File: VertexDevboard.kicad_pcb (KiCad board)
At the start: 2 copper layers, 21 x 51 mm, 33 parts, among them J1 USB_C_Receptacle_USB2.0_14P, J2 Conn_01x20, J3 Conn_01x20, J4 Conn_01x03, SW1 SW_Push, U1 RP2040, U2 MCP1700x-330xxTT, U3 W25Q128JVS, Y1 12 MHz

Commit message: DRC OK
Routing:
- net QSPI_SS: track 63.0 -> 61.0 mm
- net +3V3: track 106.9 -> 105.2 mm, vias 9 -> 8
- net GPIO23: track 11.1 -> 10.3 mm
- net GPIO22: track 7.42 -> 6.82 mm
- net XOUT: track 5.75 -> 5.22 mm
- net GPIO2: track 27.0 -> 26.5 mm
- net GPIO13: vias 3 -> 1
- net GND: vias 22 -> 21

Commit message: Before fabric
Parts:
- added G***: LOGO, LOGO, F.Cu at (127.0, 126.0)
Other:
- board text added: "Shauli Sultan"
- board text added: "Vertex DevBoard"
- board text added: "Vertex Devboard"

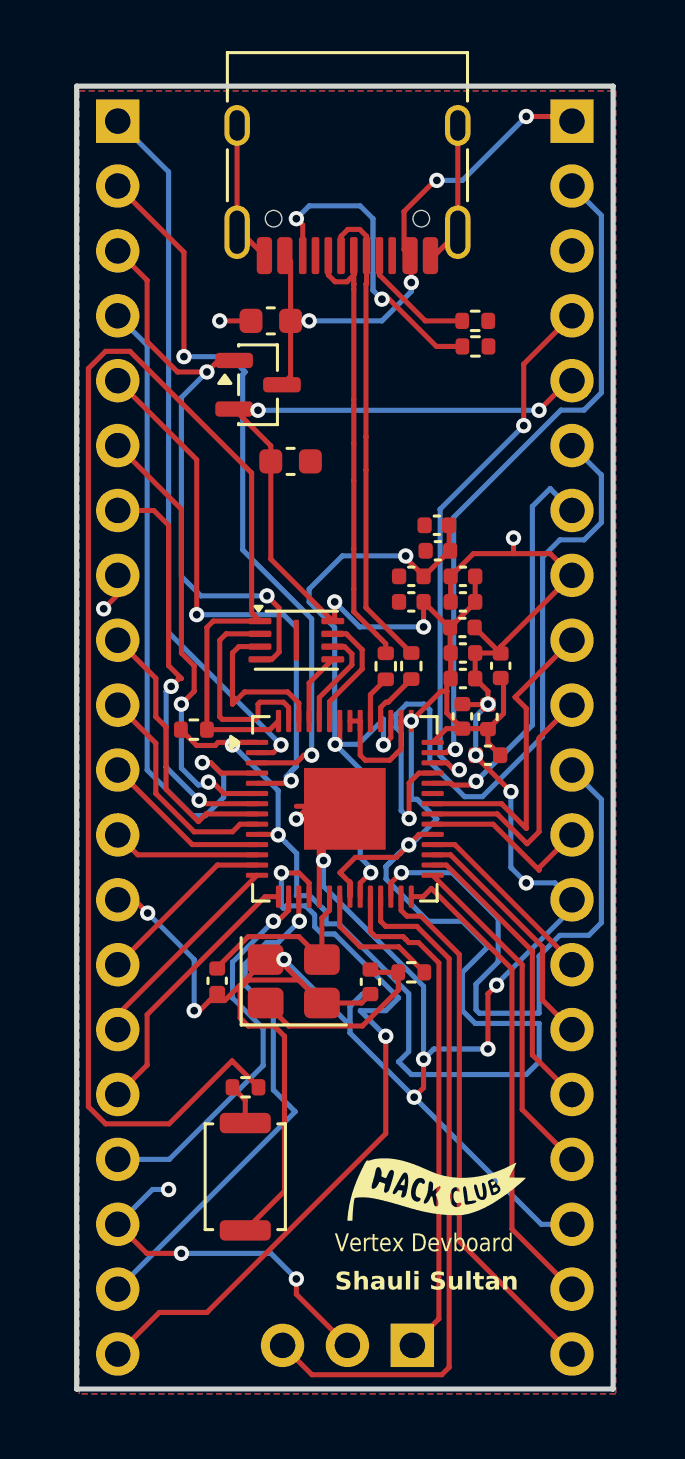
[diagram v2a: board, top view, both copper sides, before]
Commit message: Before fabric 0 DRC Erros
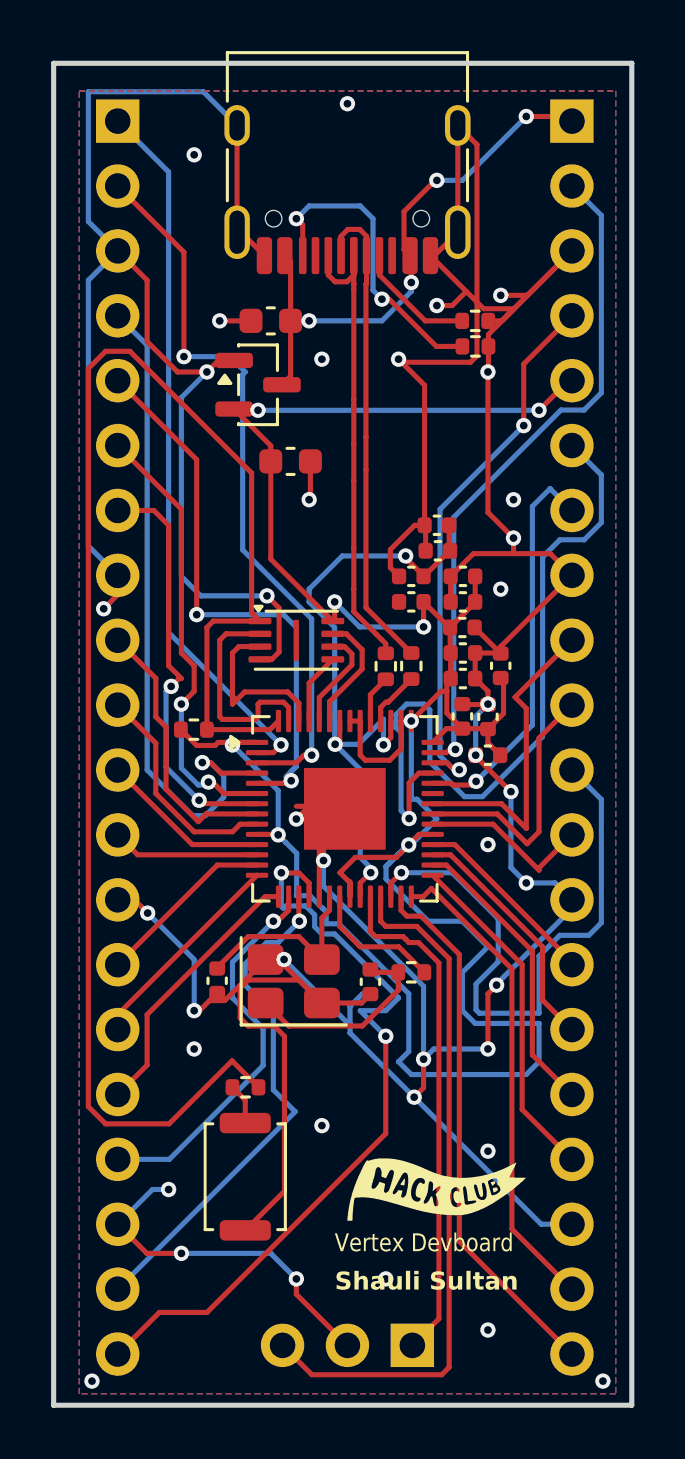
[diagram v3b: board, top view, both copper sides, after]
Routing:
- net GND: track 157.3 -> 233.6 mm, vias 21 -> 39
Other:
- board size 21 x 51 mm -> 22.6 x 52.5 mm
